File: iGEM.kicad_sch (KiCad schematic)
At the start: 30 parts

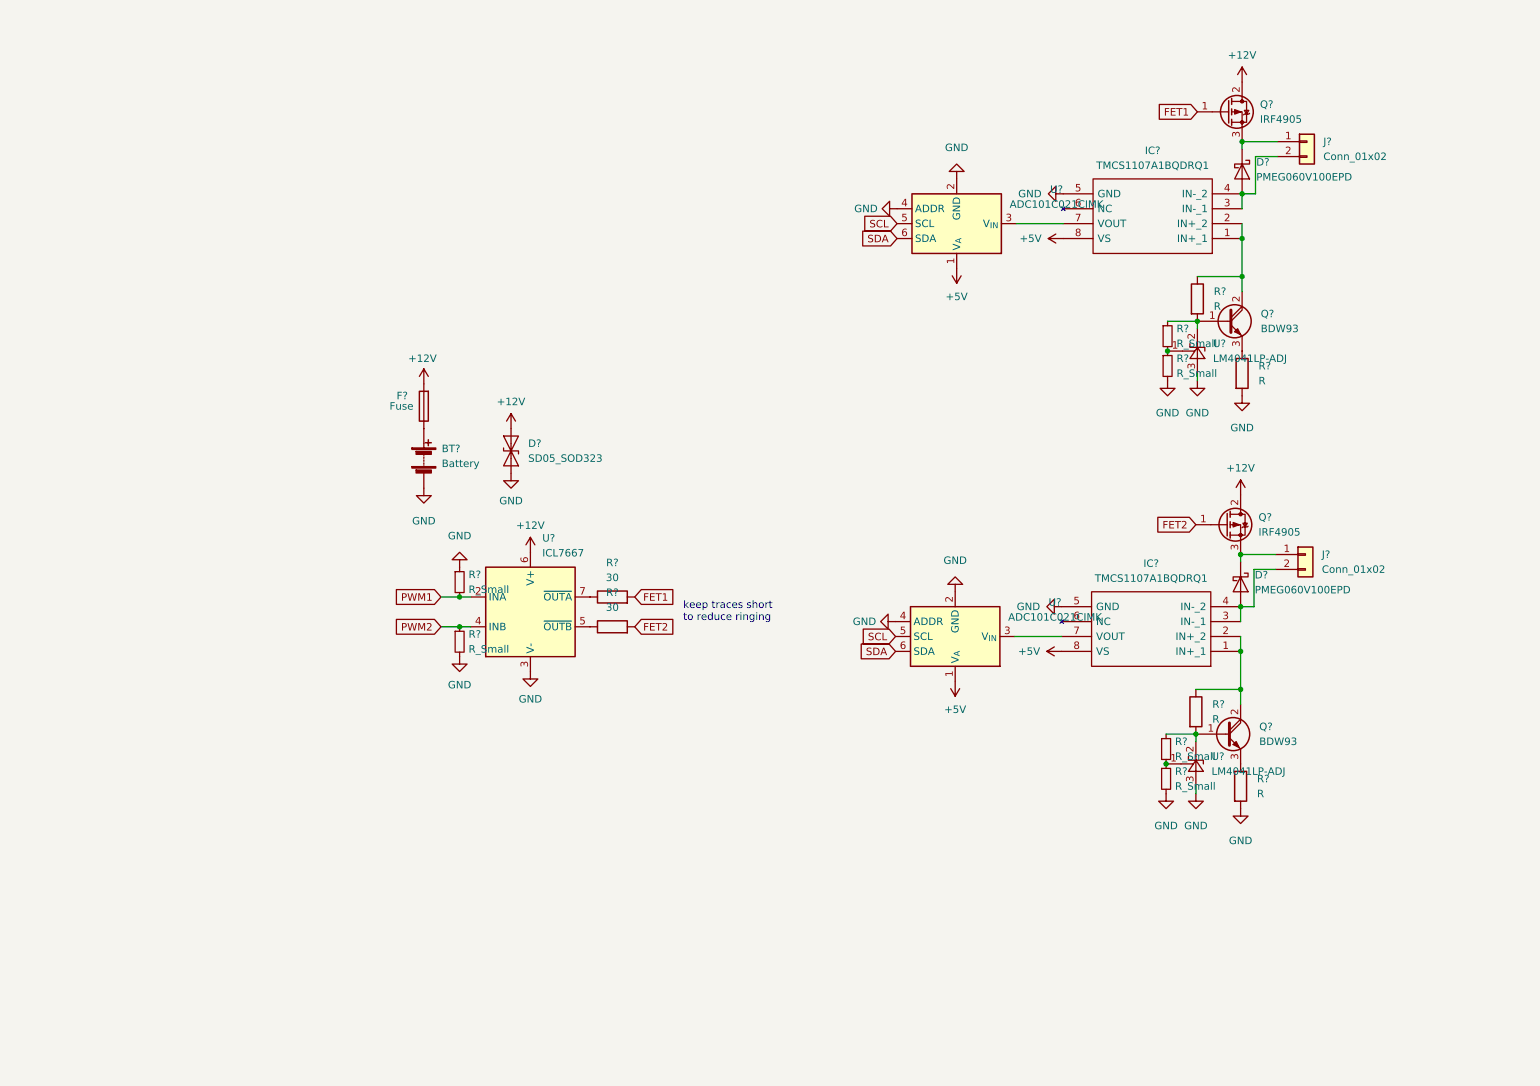
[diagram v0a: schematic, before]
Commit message: updated schematic. Added symbols for Adafruit Trinket
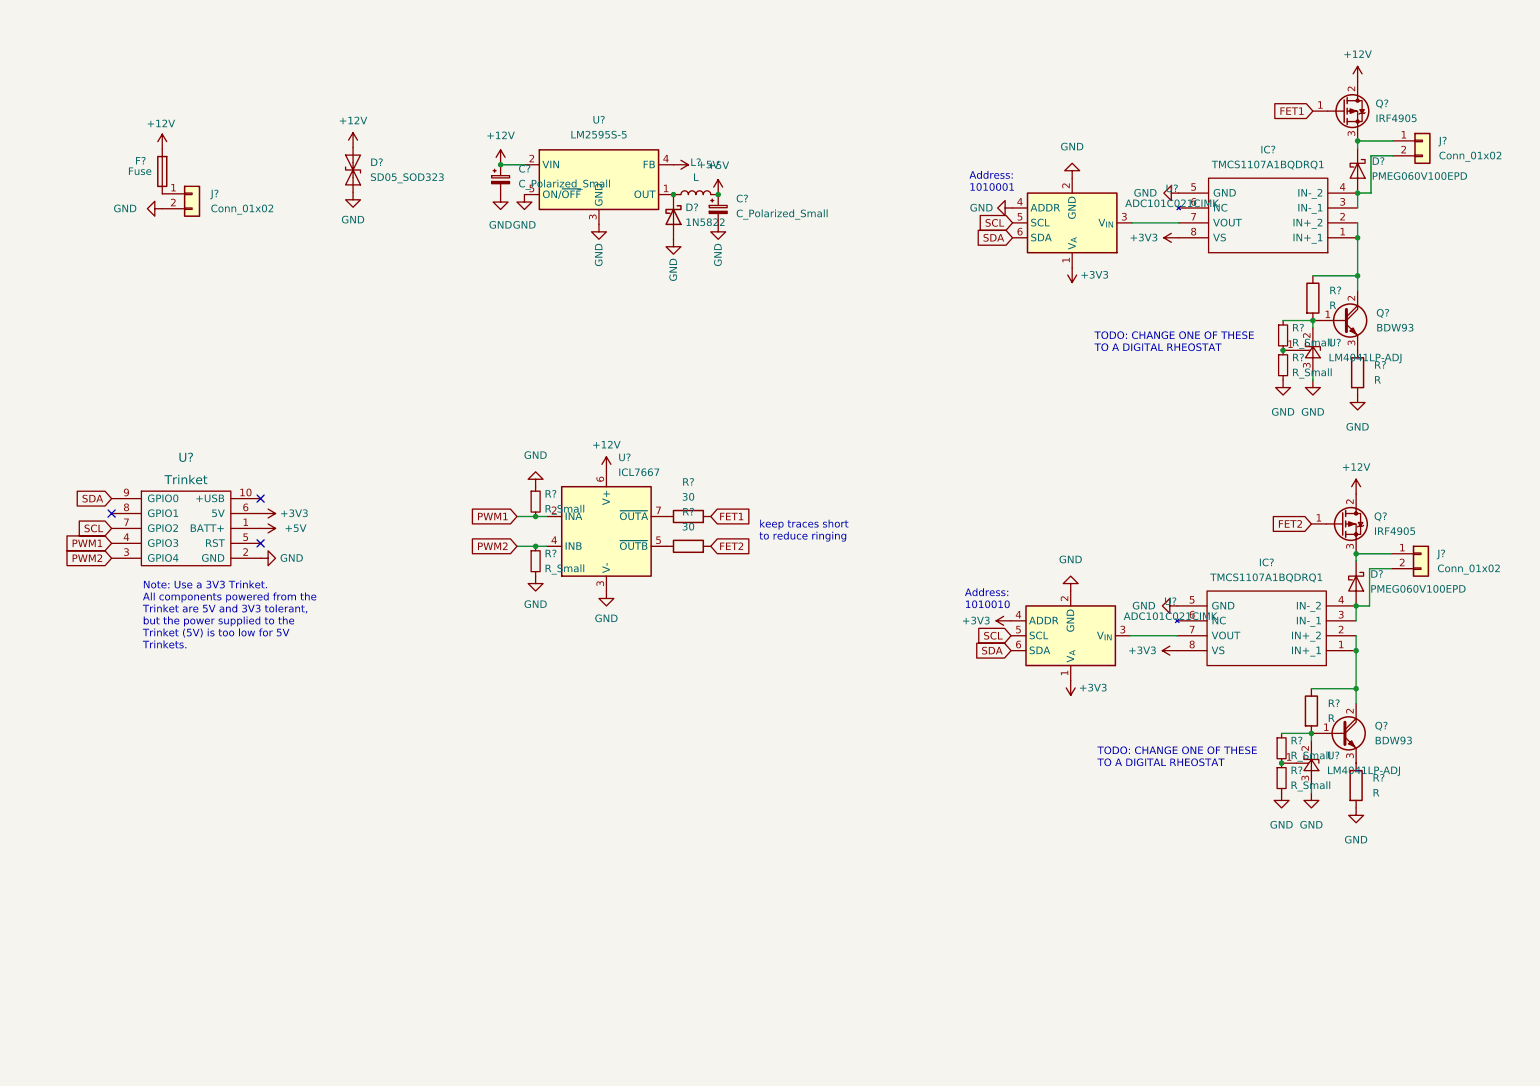
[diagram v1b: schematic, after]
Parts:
- removed BT?: Battery, symbol Device:Battery
- added C? (x2): C_Polarized_Small, symbol Device:C_Polarized_Small
- added D?: 1N5822, Diode_THT:D_DO-201AD_P15.24mm_Horizontal, symbol Diode:1N5822
- added J?: Conn_01x02, symbol Connector_Generic:Conn_01x02
- added L?: L, symbol Device:L
- added U?: LM2595S-5, Package_TO_SOT_SMD:TO-263-5_TabPin3, symbol Regulator_Switching:LM2595S-5
- added U?: Trinket, symbol SW-Adafruit:Trinket
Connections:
- net +12V: now also C?.1, U?.2 (VIN)
- net +5V: now also C?.1, L?.2, U?.1 (BATT+), U?.4 (FB); no longer IC?.8 (VS), IC?.8 (VS), U?.1 (V_{A}), U?.1 (V_{A})
- net GND: now also C?.2, C?.2, D?.2 (A), J?.2 (Pin_2), U?.2 (GND), U?.3 (GND), U?.5 (ON/~{OFF}); no longer U?.4 (ADDR)
- net PWM1: now also U?.4 (GPIO3)
- net PWM2: now also U?.3 (GPIO4)
- net SCL: now also U?.7 (GPIO2)
- net SDA: now also U?.9 (GPIO0)
- net at F?.1: now also J?.1 (Pin_1)
- new net: D?.1 (K), L?.1, U?.1 (OUT)
- new net +3V3: IC?.8 (VS), IC?.8 (VS), U?.1 (V_{A}), U?.1 (V_{A}), U?.4 (ADDR), U?.6 (5V)
- no-connect marks 0 -> 3
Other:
- note added: "Address: 1010001"
- note added: "Address: 1010010"
- note added: "Note: Use a 3V3 Trinket. All components powered from the Trinket are 5V and 3V3 tolerant, but the power supplied to the Trinket (5V) is too low for 5V Trinkets."
- note added: "TODO: CHANGE ONE OF THESE TO A DIGITAL RHEOSTAT"
- moved on the sheet: D?, F?, IC?, J?, Q?, R?, U?

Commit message: Updated schematic using simulation results and common resistor values. Now using an NPN darlington to drive a D44VH
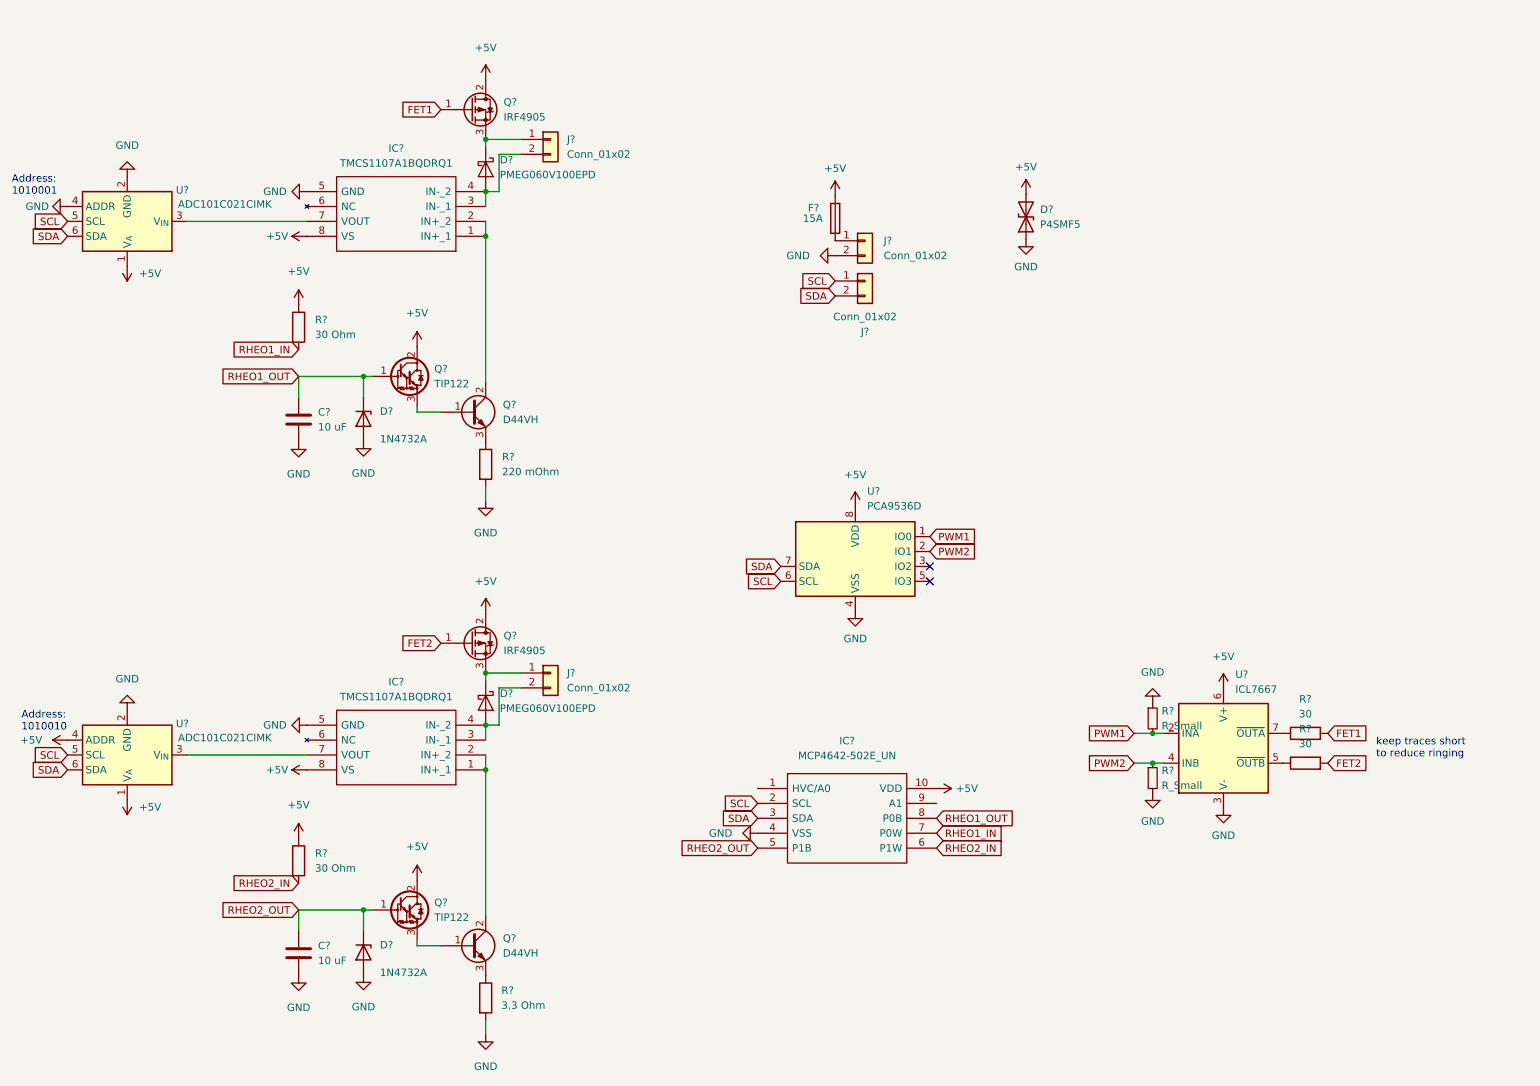
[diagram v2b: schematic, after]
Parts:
- removed C? (x2): C_Polarized_Small, symbol Device:C_Polarized_Small
- removed D?: SD05_SOD323, Diode_SMD:D_SOD-323, symbol Diode:SD05_SOD323
- removed D?: PMEG060V100EPD, Package_TO_SOT_SMD:Nexperia_CFP15_SOT-1289, symbol Diode:PMEG060V100EPD
- removed D?: 1N5822, Diode_THT:D_DO-201AD_P15.24mm_Horizontal, symbol Diode:1N5822
- removed IC?: TMCS1107A1BQDRQ1, SOIC127P600X175-8N, symbol TMCS1107A1BQDRQ1:TMCS1107A1BQDRQ1
- removed J?: Conn_01x02, symbol Connector_Generic:Conn_01x02
- removed L?: L, symbol Device:L
- removed Q? (x2): BDW93, Package_TO_SOT_THT:TO-220-3_Vertical, symbol Transistor_BJT:BDW93
- removed Q?: IRF4905, Package_TO_SOT_THT:TO-220-3_Vertical, symbol Transistor_FET:IRF4905
- removed R? (x4): R_Small, symbol Device:R_Small
- removed R? (x2): R, symbol Device:R
- removed U?: LM2595S-5, Package_TO_SOT_SMD:TO-263-5_TabPin3, symbol Regulator_Switching:LM2595S-5
- removed U?: Trinket, symbol SW-Adafruit:Trinket
- removed U? (x2): LM4041LP-ADJ, Package_TO_SOT_THT:TO-92_Inline, symbol Reference_Voltage:LM4041LP-ADJ
- removed U?: ADC101C021CIMK, Package_TO_SOT_SMD:SOT-23-6, symbol Analog_ADC:ADC101C021CIMK
- added C? (x2): 10 uF, symbol Device:C
- added D?: PMEG060V100EPD, Package_TO_SOT_SMD:Nexperia_CFP15_SOT-1289, symbol Diode:PMEG060V100EPD
- added D? (x2): 1N4732A, Diode_THT:D_DO-41_SOD81_P10.16mm_Horizontal, symbol Diode:1N47xxA
- added D?: P4SMF5, symbol Device:D_TVS
- added IC?: TMCS1107A1BQDRQ1, SOIC127P600X175-8N, symbol TMCS1107A1BQDRQ1:TMCS1107A1BQDRQ1
- added IC?: MCP4642-502E_UN, SOP50P490X110-10N, symbol MCP4642-502E_UN:MCP4642-502E_UN
- added J? (x2): Conn_01x02, symbol Connector_Generic:Conn_01x02
- added Q?: IRF4905, Package_TO_SOT_THT:TO-220-3_Vertical, symbol Transistor_FET:IRF4905
- added Q? (x2): TIP122, Package_TO_SOT_THT:TO-220-3_Vertical, symbol Transistor_BJT:TIP122
- added Q? (x2): D44VH, Package_TO_SOT_THT:TO-220-3_Vertical, symbol Device:Q_NPN_BCE
- added R?: 220 mOhm, symbol Device:R
- added R?: 30 Ohm, symbol Device:R
- added U?: PCA9536D, Package_SO:SOIC-8_3.9x4.9mm_P1.27mm, symbol Interface_Expansion:PCA9536D
- added U?: ADC101C021CIMK, Package_TO_SOT_SMD:SOT-23-6, symbol Analog_ADC:ADC101C021CIMK
- F?: value Fuse -> 15A
- R?: value R -> 30 Ohm
- R?: value R -> 3.3 Ohm
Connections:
- net +12V is gone; now on net +5V: F?.2, Q?.2 (D), U?.6 (V+)
- net +3V3 is gone; now on net +5V: IC?.8 (VS), U?.1 (V_{A}), U?.4 (ADDR)
- net +5V: now also R?.1, D?.2 (A2), IC?.10 (VDD), IC?.8 (VS), Q?.2 (C), Q?.2 (C), Q?.2 (D), R?.1, U?.1 (V_{A}), U?.8 (VDD)
- net FET1: now also Q?.1 (G)
- net GND: now also C?.2, C?.2, D?.1 (A1), D?.2 (A), D?.2 (A), IC?.4 (VSS), IC?.5 (GND), R?.2, U?.2 (GND), U?.4 (ADDR), U?.4 (VSS)
- net PWM1: now also U?.1 (IO0)
- net PWM2: now also U?.2 (IO1)
- net SCL: now also IC?.2 (SCL), J?.1 (Pin_1), U?.5 (SCL), U?.6 (SCL)
- net SDA: now also IC?.3 (SDA), J?.2 (Pin_2), U?.6 (SDA), U?.7 (SDA)
- net RHEO2_IN: now reaches R?.2
- net RHEO2_IN: now also IC?.6 (P1W)
- net at IC?.1 (IN+_1), IC?.2 (IN+_2): now also Q?.2 (C); no longer R?.1
- net at R?.1: now also Q?.3 (E)
- new net: D?.3 (K), J?.1 (Pin_1), Q?.3 (S)
- new net: D?.1 (A), D?.2 (A), IC?.3 (IN-_1), IC?.4 (IN-_2), J?.2 (Pin_2)
- new net: Q?.3 (E), R?.1
- new net: Q?.1 (B), Q?.3 (E) (x2)
- new net: IC?.7 (VOUT), U?.3 (V_{IN})
- new net: IC?.1 (IN+_1), IC?.2 (IN+_2), Q?.2 (C)
- new net RHEO1_IN: IC?.7 (P0W), R?.2
- new net RHEO1_OUT: C?.1, D?.1 (K), IC?.8 (P0B), Q?.1 (B)
- new net RHEO2_OUT: C?.1, D?.1 (K), IC?.5 (P1B), Q?.1 (B)
- no-connect marks 3 -> 2
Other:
- note removed: "Note: Use a 3V3 Trinket. All components powered from the Trinket are 5V and 3V3 tolerant, but the power supplied to the Trinket (5V) is too low for 5V Trinkets."
- note removed: "TODO: CHANGE ONE OF THESE TO A DIGITAL RHEOSTAT"
- moved on the sheet: D?, F?, IC?, J?, Q?, R?, U?

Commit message: changes made to satisfy ERC
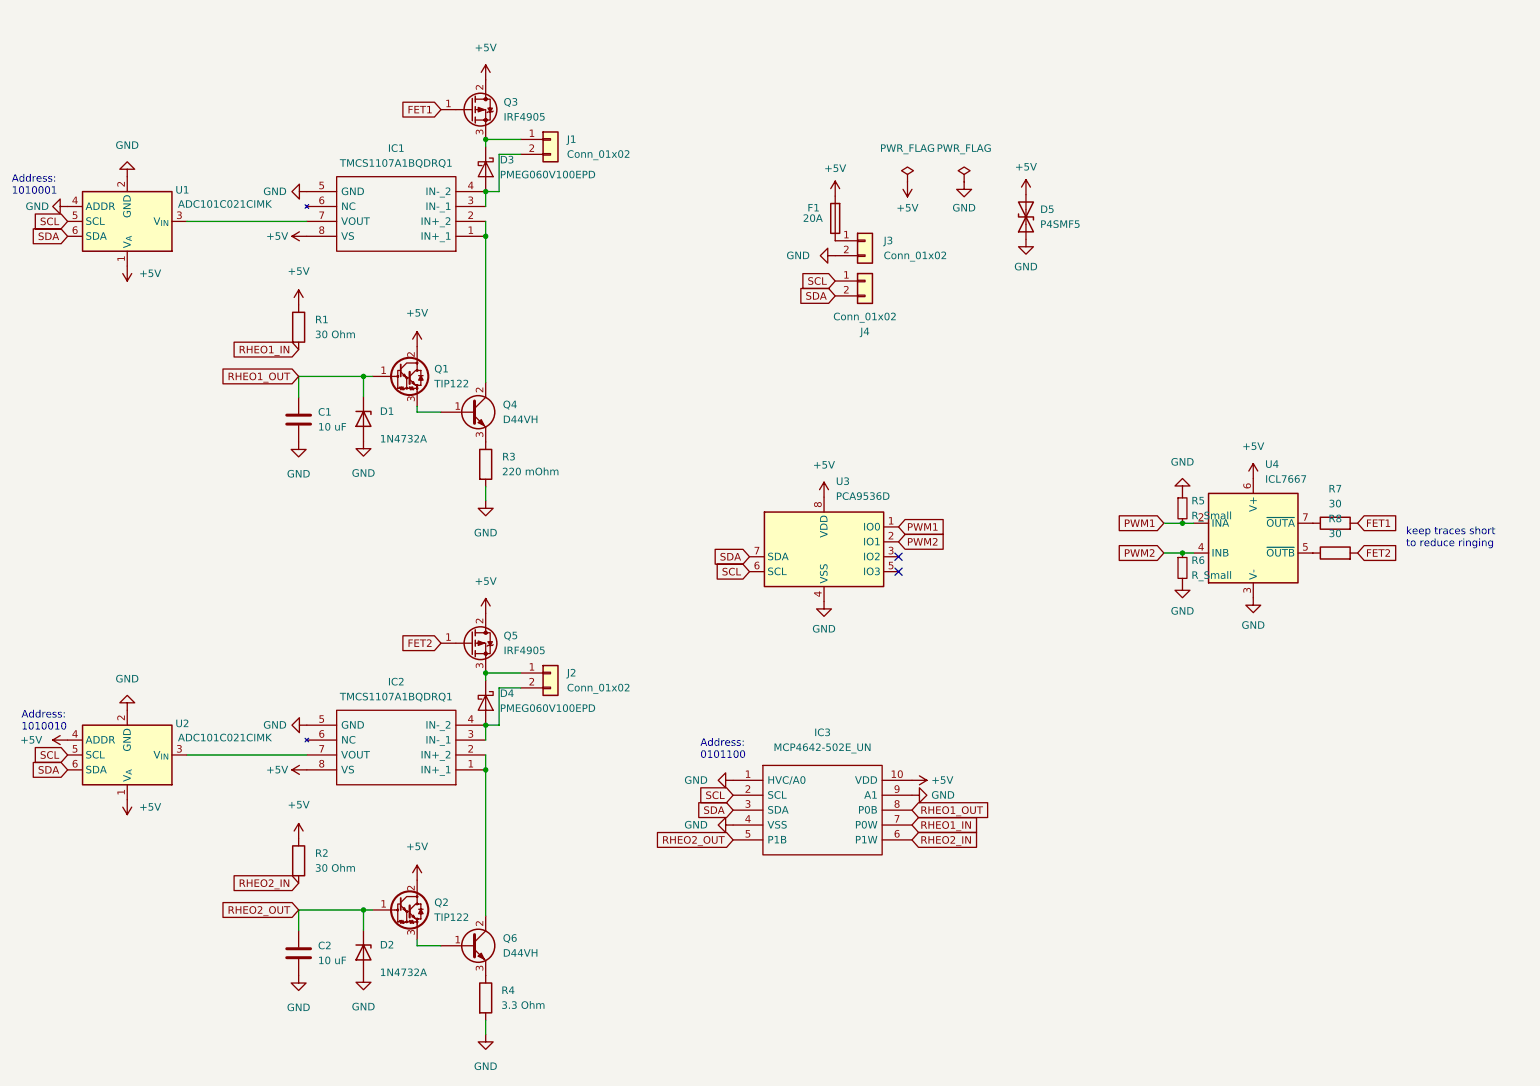
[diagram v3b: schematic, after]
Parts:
- F1: renamed from F?; value 15A -> 20A
- IC1: renamed from IC?; footprint SOIC127P600X175-8N -> TMCS1107A1BQDRQ1:SOIC127P600X175-8N
- IC2: renamed from IC?; footprint SOIC127P600X175-8N -> Package_SO:SOIC-8_3.9x4.9mm_P1.27mm
- IC3: renamed from IC?; footprint SOP50P490X110-10N -> Package_SO:MSOP-10_3x3mm_P0.5mm
- gave numbers to parts that had none: 29
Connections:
- net GND: now also IC3.1 (HVC/A0), IC3.9 (A1)
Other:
- note added: "Address: 0101100"
- moved on the sheet: IC3, R5, R6, R7, R8, U3, U4
